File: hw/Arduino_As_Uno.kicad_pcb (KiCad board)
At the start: 2 copper layers, 68.6 x 53.3 mm, 66 parts, among them CON1 BARREL_JACK, IC1 FDG6331L, P1 USB_OTG, P10 CONN_01X06, P11 CONN_01X08, P2 CONN_02X03_ICSP, P3 CONN_02X03, P4 CONN_02X03_ICSP, P5 CONN_01X08, P6 CONN_02X03, P7 CONN_02X03_ICSP, P8 CONN_02X03_ICSP, P9 CONN_01X10, Q1 FDN340P, SW1 SW_PUSH, U1 LM2940LD-5.0, U10 TS3A44159, U2 MIC5205, U3 ATMEGA16U2, U4 23K256, U5 ATTINY85-SUR, U6 TS3A44159, U7 ATMEGA328PB-MU, U8 74LVCH1T45, U9 ATTINY85-SUR, X1 CRYSTAL, X2 RESONATOR

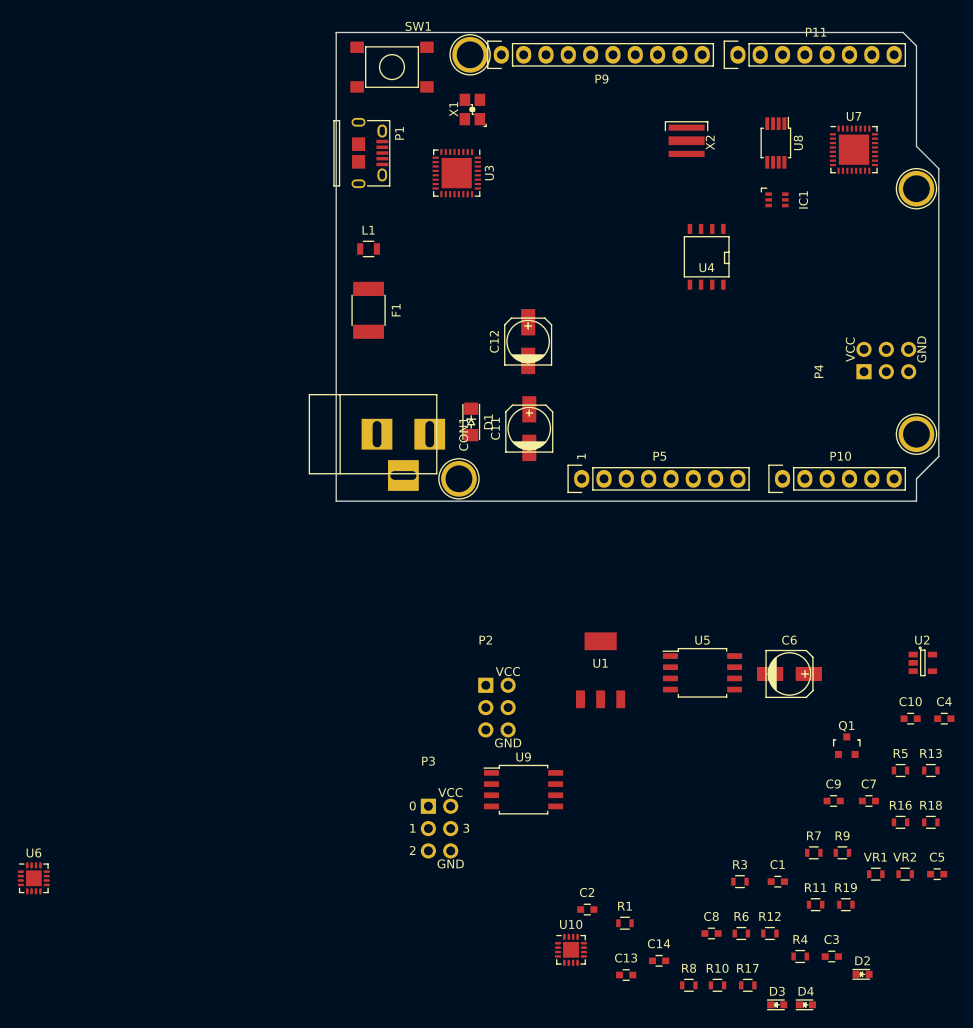
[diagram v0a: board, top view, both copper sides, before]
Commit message: Coarse placement of power and usb passives. All components are on board. Connectors have the correct footprint. Tinys need better placement. Final adjustments will make placing traces easier.
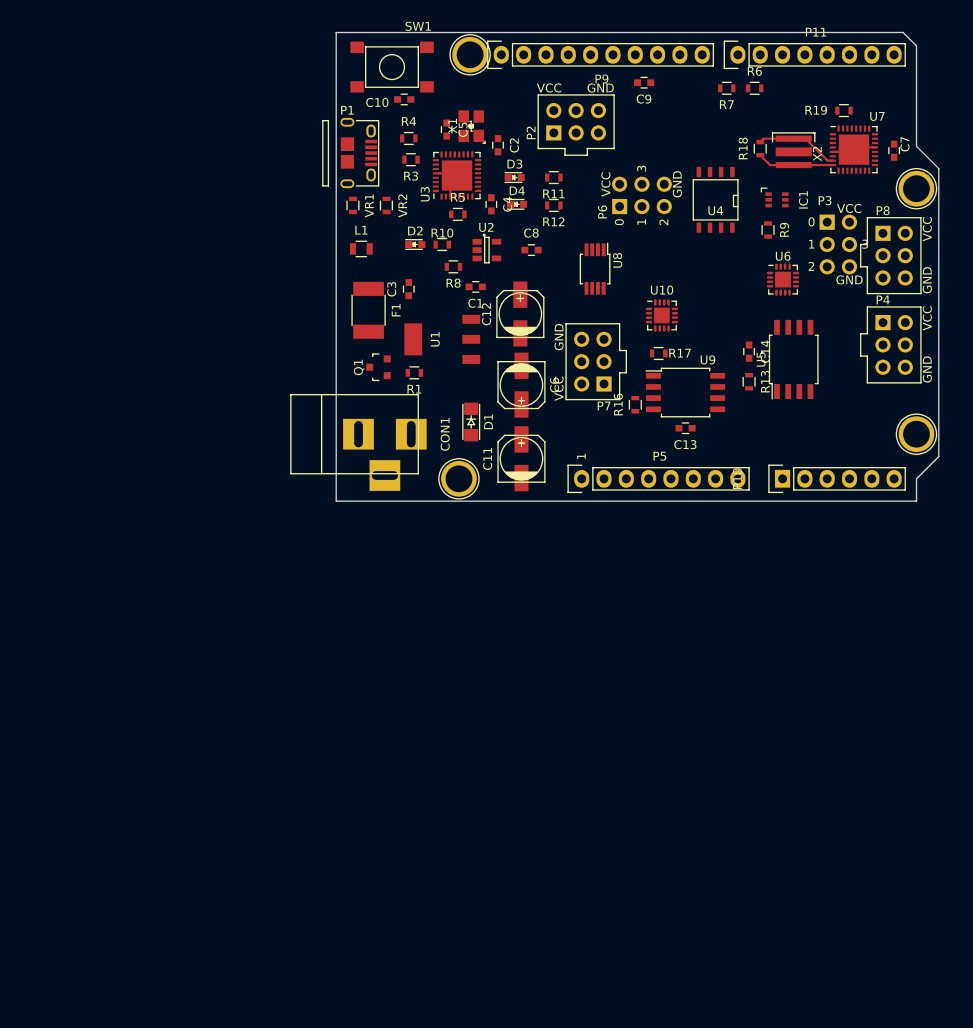
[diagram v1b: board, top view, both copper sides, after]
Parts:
- added P6: CONN_02X03, pcbfp_lib:Pin_Header_Straight_2x03_ATTINY, F.Cu at (143.3, 92.8)
- added P7: CONN_02X03_ICSP, pcbfp_lib:Pin_Header_Straight_2x03_ICSP, F.Cu at (141.5, 113.0)
- added P8: CONN_02X03_ICSP, pcbfp_lib:Pin_Header_Straight_2x03_ICSP, F.Cu at (173.2, 95.9)
- C9: value 100n -> .1uF
- P10: footprint pcbfp_lib:Socket_Strip_Arduino_1x06 -> Pin_Headers:Pin_Header_Straight_1x06
- moved U6 109.1 mm to (161.9, 101.2)
- moved R4 103.2 mm to (119.3, 85.1)
- moved C5 101.5 mm to (123.6, 84.1), turned to 270 degrees
- moved D3 98.8 mm to (131.3, 89.5)
- moved D2 97.4 mm to (120.0, 97.2)
- moved D4 96.9 mm to (131.6, 92.6)
- moved VR1 96.6 mm to (112.9, 92.7), turned to 270 degrees
- moved VR2 96.3 mm to (116.7, 92.7), turned to 270 degrees
- moved R6 96.2 mm to (158.6, 79.4)
- moved C10 91.0 mm to (118.7, 80.6)
- moved R19 90.4 mm to (168.8, 81.9)
- moved R3 90.3 mm to (119.5, 87.5), turned to 180 degrees
- moved R10 89.9 mm to (123.1, 97.2)
- moved C3 89.9 mm to (119.3, 102.2), turned to 90 degrees
- moved R11 88.0 mm to (135.8, 89.5), turned to 180 degrees
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- renumbered P8 to P12, P6 to P13, P7 to P14, P5 to P15
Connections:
- X1 pad 2: Net-(X1-Pad2) -> GND
- X1 pad 4: Net-(X1-Pad4) -> GND
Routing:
- net GND: track 0.00 -> 20.8 mm
- net /RES1_328: track 0.00 -> 9.81 mm
- net /RES2_328: track 0.00 -> 8.73 mm

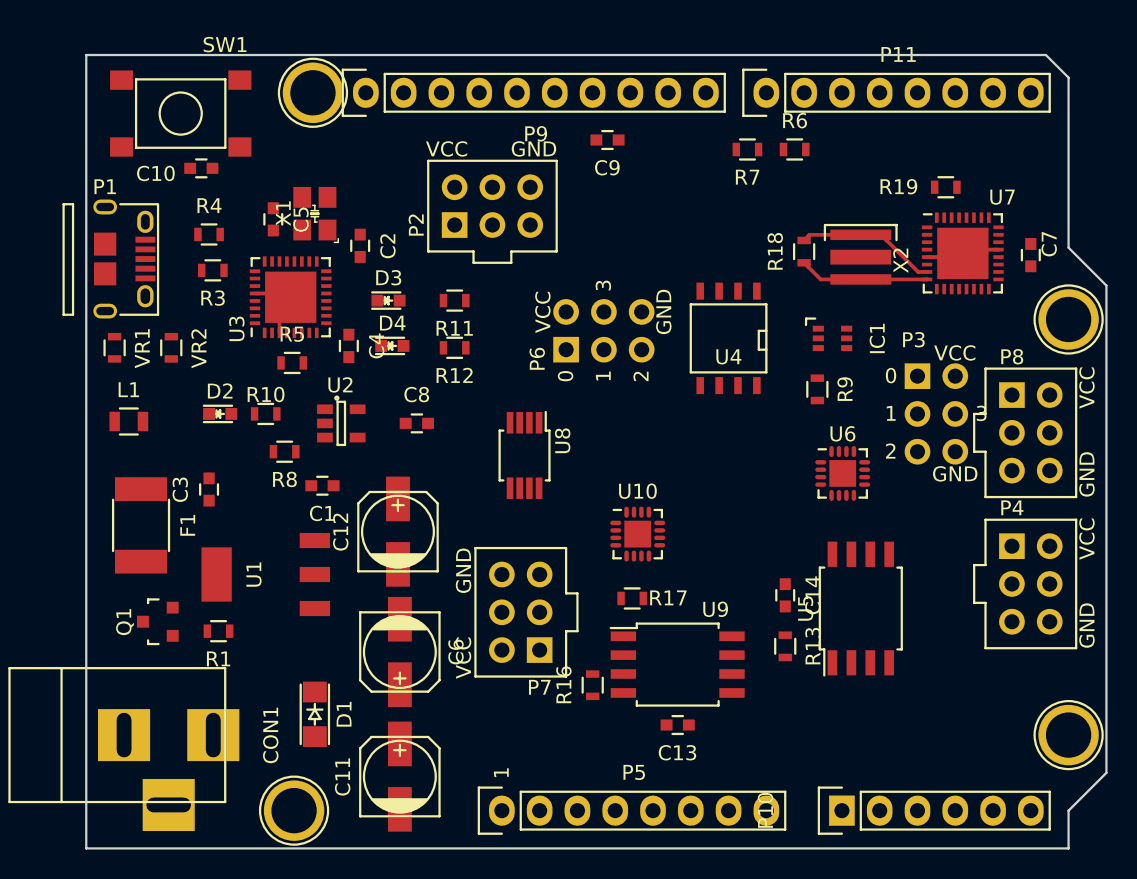
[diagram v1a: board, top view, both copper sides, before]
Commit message: Semi-Final PCB layout. Missing R1 for load switch. Pre-traces
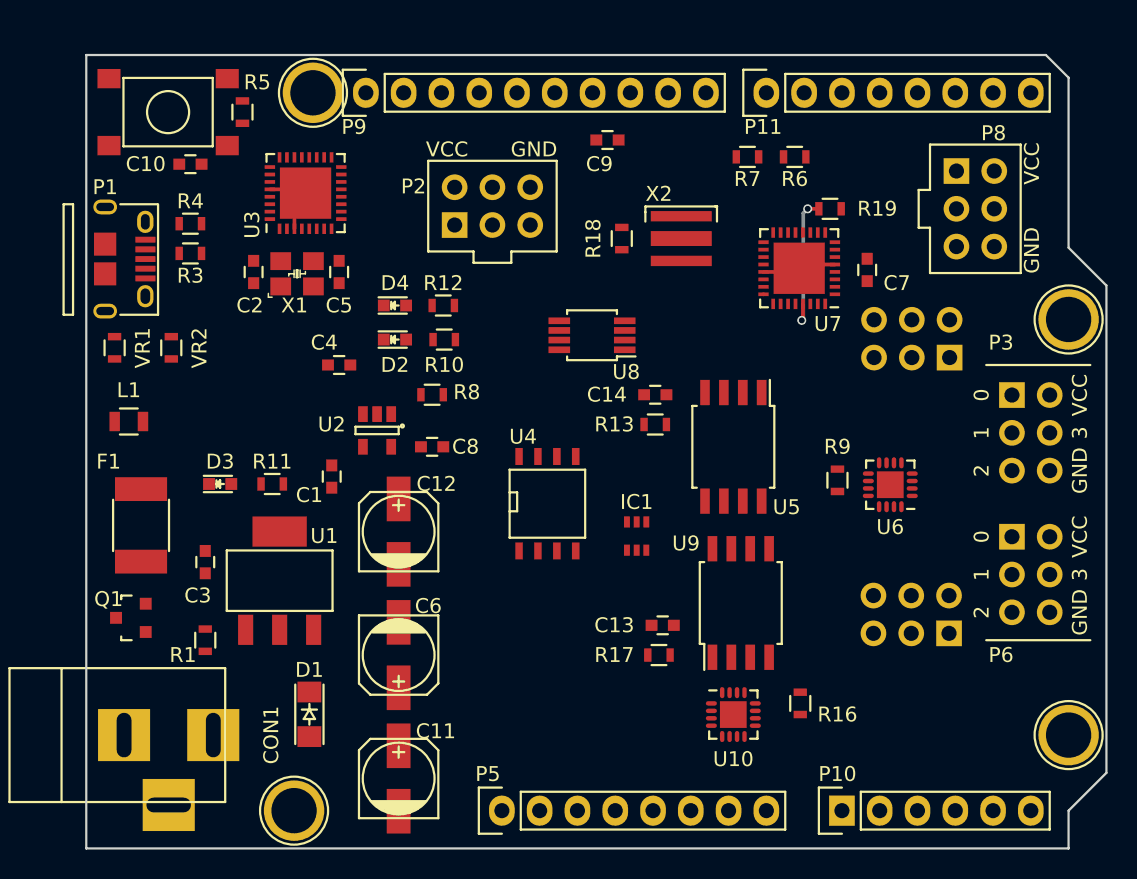
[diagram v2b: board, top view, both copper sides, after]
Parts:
- IC1: footprint TO_SOT_Packages_SMD:SC-70-6 -> pcbfp_lib:SC-70-6
- P4, P7: moved to B.Cu
- moved P6 32.5 mm to (173.2, 105.4), turned to 0 degrees
- moved P7 27.5 mm to (169.0, 111.9), turned to 90 degrees
- moved IC1 18.7 mm to (148.0, 105.4), turned to 0 degrees
- moved R11 17.4 mm to (123.5, 101.9)
- moved R13 17.3 mm to (149.2, 97.9), turned to 0 degrees
- moved R5 17.2 mm to (121.5, 76.9), turned to 90 degrees
- moved D3 16.7 mm to (120.0, 101.9)
- moved U4 16.5 mm to (142.0, 103.2), turned to 0 degrees
- moved C14 16.1 mm to (149.2, 95.9), turned to 0 degrees
- moved P8 15.5 mm to (169.5, 80.8)
- moved R16 14.0 mm to (159.0, 116.6)
- moved U5 13.8 mm to (154.5, 99.4), turned to 270 degrees
- moved U10 13.7 mm to (154.5, 117.4)
- moved P4 13.4 mm to (169.0, 93.4), turned to 90 degrees
- moved R10 13.0 mm to (135.1, 92.2)
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- renumbered P12 to P22
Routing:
- net /RES1_328: track 9.81 -> 0.00 mm
- net /RST_328: track 0.00 -> 9.55 mm, vias 0 -> 2
- net /RES2_328: track 8.73 -> 0.01 mm
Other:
- board text removed: "1"

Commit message: Pre review commit. About 25% routed. Mostly Power.
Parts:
- U2: footprint TO_SOT_Packages_SMD:SOT-23-5 -> pcbfp_lib:SOT-23-5
- moved D3 15.5 mm to (131.7, 91.8)
- moved R11 15.3 mm to (135.0, 91.8)
- moved C4 14.2 mm to (121.0, 81.5), turned to 270 degrees
- moved D2 10.2 mm to (121.7, 94.2)
- moved R10 10.2 mm to (125.1, 94.2)
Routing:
- net Net-(L1-Pad1): track 0.00 -> 22.3 mm, vias 0 -> 2
- net Net-(F1-Pad1): track 0.00 -> 18.3 mm
- net Net-(CON1-Pad3): track 0.00 -> 16.2 mm
- net Net-(P1-Pad3): track 0.00 -> 13.1 mm, vias 0 -> 2
- net Net-(CON1-Pad2): track 0.00 -> 12.8 mm
- net Net-(P1-Pad2): track 0.00 -> 12.5 mm, vias 0 -> 4
- net /TXLED: track 0.00 -> 8.37 mm
- net +5V: track 0.00 -> 7.44 mm
- net Net-(CON1-Pad1): track 0.00 -> 6.50 mm
- net Net-(R3-Pad1): track 0.00 -> 6.29 mm
- net Net-(R4-Pad2): track 0.00 -> 5.13 mm, vias 0 -> 2
- net /RES2_U2: track 0.00 -> 4.77 mm
- net /USBVCC: track 0.00 -> 4.47 mm
- net Net-(C4-Pad1): track 0.00 -> 2.69 mm
- net /RES1_U2: track 0.00 -> 1.91 mm
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
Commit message: The actual pre meeting commit.
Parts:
- moved R18 13.5 mm to (158.8, 91.9), turned to 0 degrees
- moved X2 8.37 mm to (158.7, 88.5), turned to 0 degrees
- moved R19 7.08 mm to (153.9, 84.0)
- moved U7 7.08 mm to (151.9, 88.0)
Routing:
- net +3V3: track 0.00 -> 49.1 mm
- net +5V: track 7.44 -> 42.7 mm, vias 0 -> 2
- net /RES2_328: track 0.00 -> 12.0 mm
- net /MOSI_RAM: track 0.00 -> 9.89 mm
- net /SCK_RAM: track 0.00 -> 9.33 mm
- net /RES1_328: track 0.00 -> 8.94 mm
- net /VIN: track 0.00 -> 7.50 mm
- net /3.3V_UNSAFE: track 0.00 -> 2.65 mm

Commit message: Fix layout.
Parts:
- P4, P7: moved to F.Cu
- moved C7 16.1 mm to (147.4, 87.5), turned to 270 degrees
- moved R9 12.1 mm to (151.1, 95.4), turned to 0 degrees
- moved U6 10.1 mm to (156.3, 96.8)
- moved R16 9.67 mm to (149.4, 117.8), turned to 180 degrees
- moved P4 8.59 mm to (161.9, 98.2)
- moved U9 8.23 mm to (156.6, 117.9), turned to 0 degrees
- moved P7 7.40 mm to (161.7, 110.6)
- moved R17 6.50 mm to (149.4, 119.9)
- moved R18 6.42 mm to (162.2, 86.5), turned to 90 degrees
- moved U10 6.17 mm to (156.6, 111.6)
- moved VR1 5.80 mm to (117.7, 89.5)
- moved U5 5.67 mm to (153.6, 105.0), turned to 0 degrees
- moved IC1 5.08 mm to (144.8, 109.3)
- moved R5 4.70 mm to (123.8, 81.0), turned to 0 degrees
- moved VR2 4.51 mm to (119.9, 89.5)
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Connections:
- net Net-(P1-Pad2) renamed /D_N
- net Net-(P1-Pad3) renamed /D_P
- net Net-(R3-Pad1) renamed /D+
- net Net-(R4-Pad2) renamed /D-
- U3 pad 33: (no net) -> GND
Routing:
- net +3V3: track 49.1 -> 35.2 mm
- net +5V: track 42.7 -> 32.1 mm
- net /MOSI_RAM: track 9.89 -> 0.00 mm
- net /SCK_RAM: track 9.33 -> 0.00 mm
- net /TXLED: track 8.37 -> 0.00 mm
- net /RST_328: track 9.55 -> 17.5 mm
- net /D+: track 6.29 -> 0.00 mm
- net /VIN: track 7.50 -> 1.44 mm
- net /D_P: track 13.1 -> 7.09 mm, vias 2 -> 0
- net /D-: track 5.13 -> 0.00 mm, vias 2 -> 0
- net /RES1_U2: track 1.91 -> 6.66 mm
- net /D_N: track 12.5 -> 8.30 mm, vias 4 -> 2
- net Net-(C4-Pad1): track 2.69 -> 0.00 mm
- net /3.3V_UNSAFE: track 2.65 -> 0.00 mm
- net Net-(D3-Pad2): track 0.00 -> 1.80 mm
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
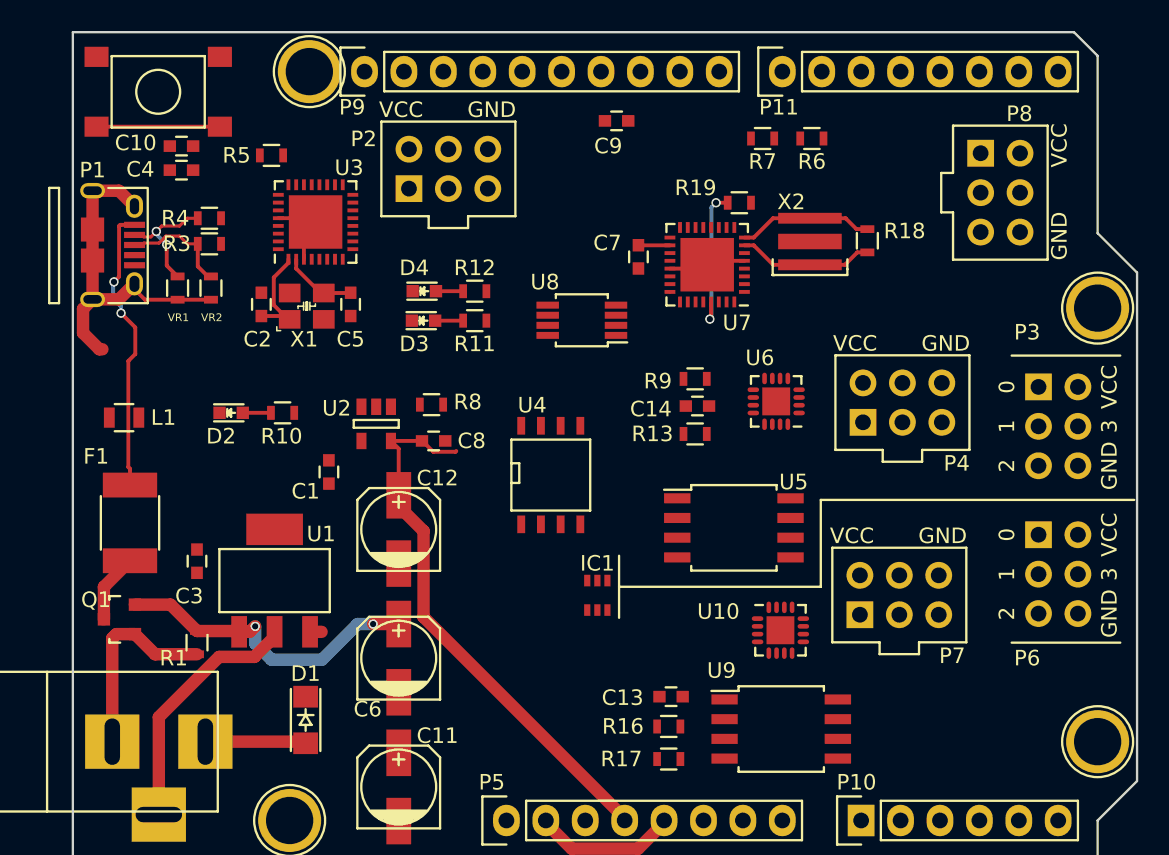
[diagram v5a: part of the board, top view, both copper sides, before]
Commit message: No major changes. PCB is 50% routed with clear vert/horiz pattern. This is just a restore point.
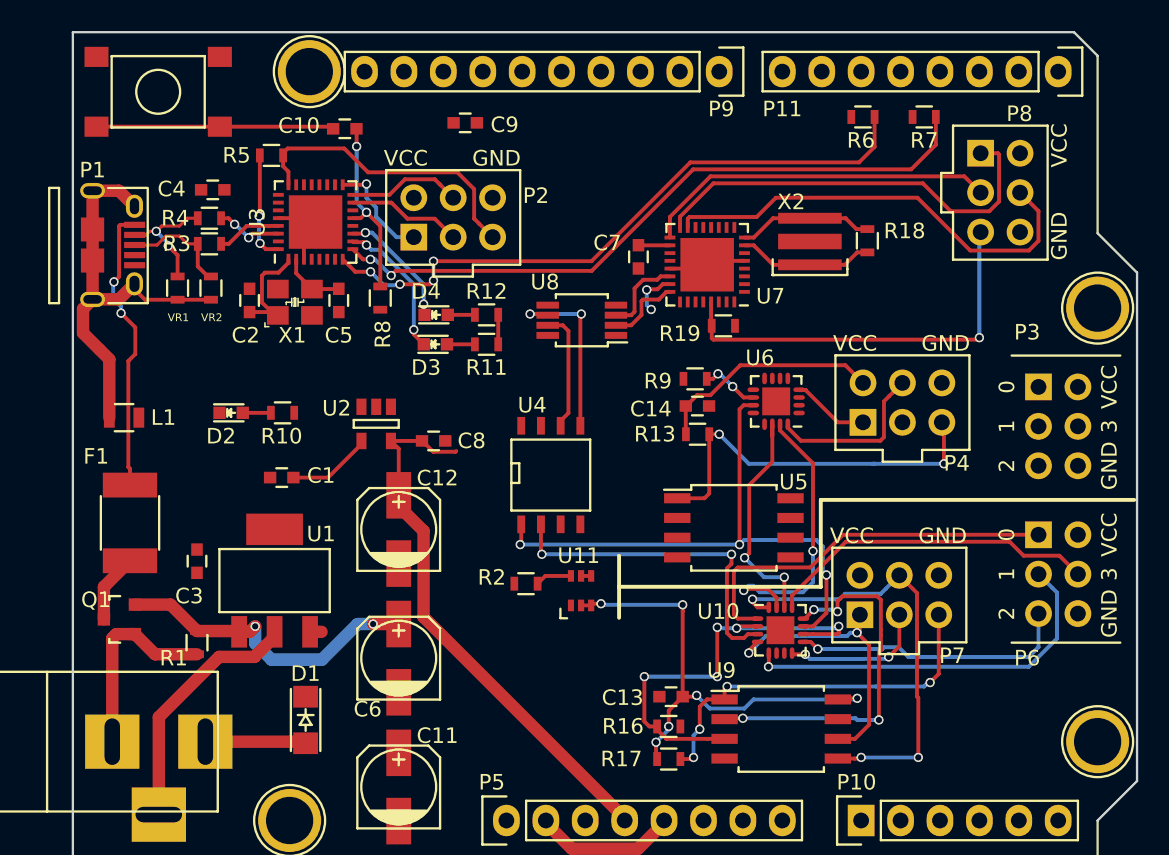
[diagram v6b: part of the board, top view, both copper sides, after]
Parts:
- removed IC1: FDG6331L, pcbfp_lib:SC-70-6
- added R2: 1K, Resistors_SMD:R_0603, F.Cu at (140.2, 108.6)
- added U11: FDG6331L, TO_SOT_Packages_SMD:SC-70-6, F.Cu at (143.7, 109.0)
- moved P9 22.9 mm to (152.7, 75.6), turned to 180 degrees
- moved P11 17.8 mm to (174.5, 75.6), turned to 180 degrees
- moved C10 10.6 mm to (128.5, 79.2)
- moved R7 10.5 mm to (165.9, 78.5), turned to 0 degrees
- moved C9 9.76 mm to (136.3, 78.9), turned to 0 degrees
- moved R19 8.00 mm to (152.9, 91.9)
- moved R8 7.62 mm to (130.8, 90.2), turned to 270 degrees
- moved R6 3.57 mm to (161.9, 78.5), turned to 180 degrees
- moved P2 3.14 mm to (133.0, 86.2)
- moved C1 3.06 mm to (124.5, 101.7), turned to 180 degrees
- moved C4 2.38 mm to (120.0, 83.2)
- moved D3 1.70 mm to (134.4, 93.1)
- moved D4 1.70 mm to (134.4, 91.2)
- moved R11 1.70 mm to (137.7, 93.1)
- moved R12 1.70 mm to (137.7, 91.2)
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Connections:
- P22 pad 1: /MISO_328 -> GND
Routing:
- net /3.3V_UNSAFE: track 0.00 -> 45.7 mm, vias 0 -> 6
- net Net-(R7-Pad2): track 0.00 -> 43.6 mm, vias 0 -> 2
- net Net-(R6-Pad1): track 0.00 -> 41.3 mm, vias 0 -> 4
- net /~SS~: track 0.00 -> 37.2 mm, vias 0 -> 3
- net /MOSI_RAM: track 0.00 -> 31.0 mm, vias 0 -> 4
- net /MOSI_328: track 0.00 -> 29.0 mm
- net /MOSI_T2: track 0.00 -> 28.9 mm, vias 0 -> 3
- net /SELECT_T2: track 0.00 -> 28.6 mm, vias 0 -> 5
- net /MISO_328: track 0.00 -> 27.4 mm
- net /~RST~_T2: track 0.00 -> 25.4 mm, vias 0 -> 4
- net /IO0_T2: track 0.00 -> 25.3 mm
- net /IO1_T2: track 0.00 -> 24.9 mm, vias 0 -> 1
- net /~RST~_T1: track 0.00 -> 24.8 mm, vias 0 -> 2
- net /RST_328: track 17.5 -> 41.8 mm, vias 2 -> 1
- net /~SS~_T2: track 0.00 -> 24.0 mm, vias 0 -> 4
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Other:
- net class Default: clearance 0.2 -> 0.15
- rule trace_clearance: 0.2 -> 0.15
- rule trace_min: 0.2 -> 0.05

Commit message: end of day commit
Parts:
- moved C9 0.67 mm to (135.6, 78.7)
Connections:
- U10 pad 17: (no net) -> GND
- U6 pad 17: (no net) -> GND
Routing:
- net /AD5/MISO1: track 3.03 -> 79.1 mm, vias 2 -> 7
- net /AD4/SCK1: track 4.99 -> 76.1 mm, vias 0 -> 3
- net /AD1: track 0.00 -> 55.2 mm, vias 0 -> 2
- net /SCK_T1: track 0.00 -> 34.9 mm, vias 0 -> 5
- net /RST_328: track 41.8 -> 76.5 mm, vias 1 -> 5
- net /IO0/RX: track 0.00 -> 33.9 mm, vias 0 -> 2
- net /AD2/SDA: track 0.00 -> 32.4 mm, vias 0 -> 2
- net /IO1/TX: track 0.00 -> 30.9 mm, vias 0 -> 4
- net /AD3/SCL: track 0.00 -> 28.5 mm, vias 0 -> 1
- net /IO2_T1: track 0.00 -> 24.7 mm, vias 0 -> 5
- net +5V: track 41.0 -> 65.3 mm, vias 4 -> 7
- net /IO2: track 0.00 -> 23.7 mm, vias 0 -> 1
- net /IO3_T1: track 0.00 -> 23.7 mm, vias 0 -> 1
- net /IO3: track 0.00 -> 21.4 mm, vias 0 -> 1
- net /MISO_RAM: track 21.6 -> 42.4 mm, vias 2 -> 4
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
